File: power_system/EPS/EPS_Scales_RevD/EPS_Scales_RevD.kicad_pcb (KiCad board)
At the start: 4 copper layers, 100 x 100 mm, 268 parts, among them CN1 DF11-16DP-2DSA(08), J1 Input Power, J10 DF11-16DP-2DSA, J18 Conn_01x04, J2 Conn_01x01_Socket, J3 Conn_01x01_Socket, J4 Conn_01x01_Socket, J5 Conn_01x01_Socket, J6 DF11-16DP-2DSA, J7 Conn_01x04, J8 Conn_01x04, U1 LT8612EUDE#PBF, U12 TPS1HB08BQPWPRQ1, U13 LT8612EUDE#PBF, U14 TLV1704, U15 TPS1HB08BQPWPRQ1, U16 INA260AIPWR, U17 TPS1HB08BQPWPRQ1, U2 INA260AIPWR, U3 LT8612EUDE#PBF, U4 TLV1704, U5 INA260AIPWR, U6 TLV1704, U7 LTC6902, U9 TCA4307DGKR

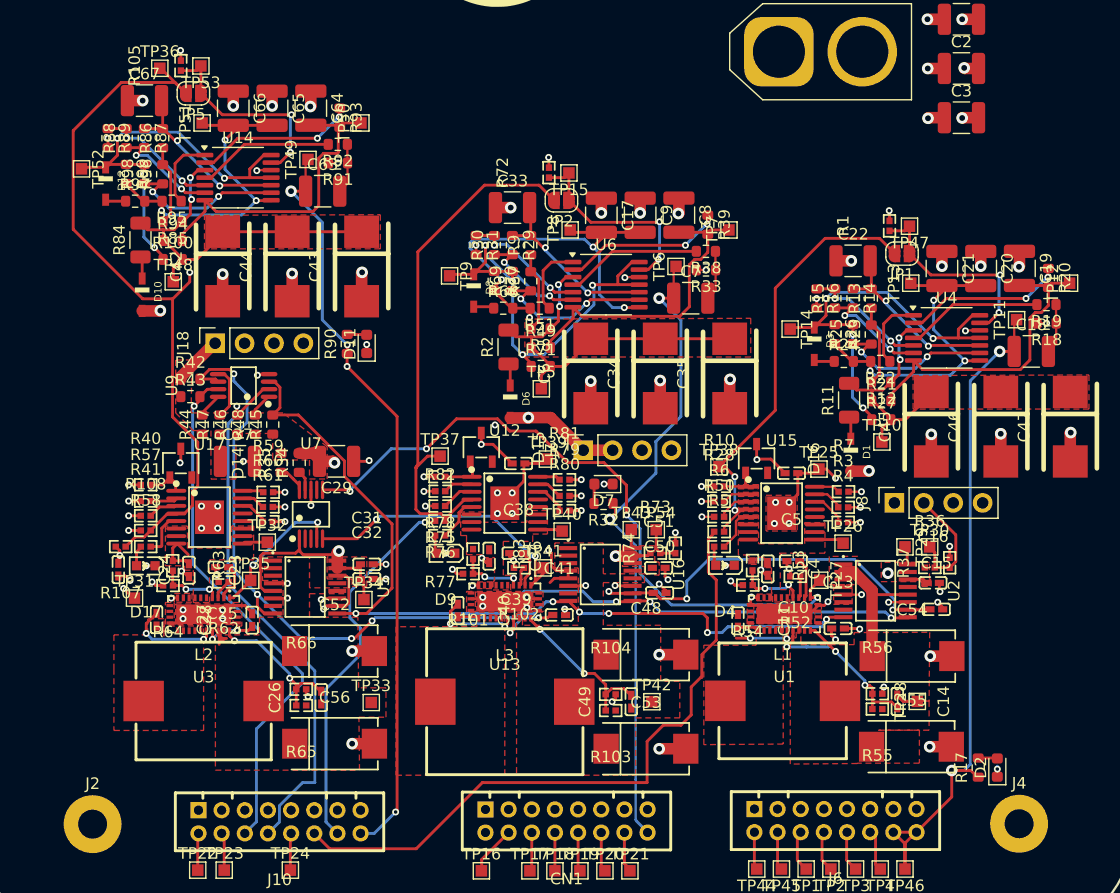
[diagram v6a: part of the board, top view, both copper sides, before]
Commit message: Cleaned up Layout
Fixed to work with JLC recommendations. Prepping for review with Andrew
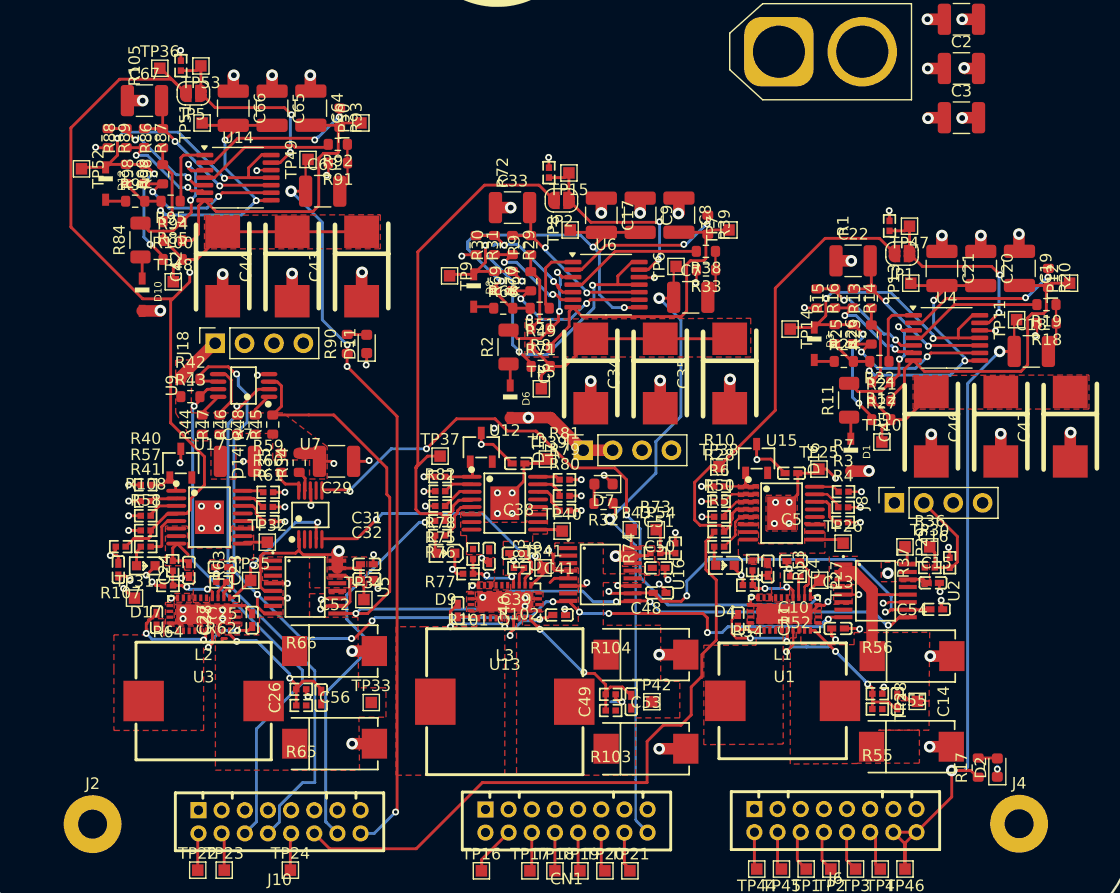
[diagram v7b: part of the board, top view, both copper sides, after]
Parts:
- moved R62 0.21 mm to (171.1, 96.1)
- moved R95 0.09 mm to (166.8, 63.2)
- moved U7 0.08 mm to (178.8, 90.3)
- moved C7 0.08 mm to (211.7, 71.5)
- moved R22 0.07 mm to (228.0, 77.0)
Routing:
- net GND: track 154.1 -> 160.4 mm, vias 116 -> 113
- net ~{WD_EN_JETSON}: track 39.1 -> 44.1 mm, vias 2 -> 0
- net Net-(U1-BST): track 5.07 -> 7.87 mm
- net Net-(U3-BIAS): track 3.77 -> 1.09 mm
- net /OBC_Subsystem/WD_OBC/WDT-VIN: track 31.9 -> 34.5 mm
- net SCL: track 79.4 -> 81.9 mm
- net /Perif_Subsystem/WD_Perif/WDT-VIN: track 32.1 -> 33.9 mm
- net Net-(U3-INTVCC): track 4.77 -> 6.46 mm
- net ~{WD_EN_OBC}: track 63.8 -> 65.4 mm
- net /Jetson_Subsystem/WD_Jetson/WDT-VIN: track 19.9 -> 21.2 mm
- net Net-(D12-K): track 35.5 -> 36.6 mm
- net +3.3V_OBC: track 113.3 -> 112.3 mm
- net Net-(U15-SEL1): track 3.02 -> 4.06 mm
- net ~{WD_EN_PERIF}: track 45.9 -> 46.9 mm
- net Net-(D3-K): track 35.5 -> 36.4 mm
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
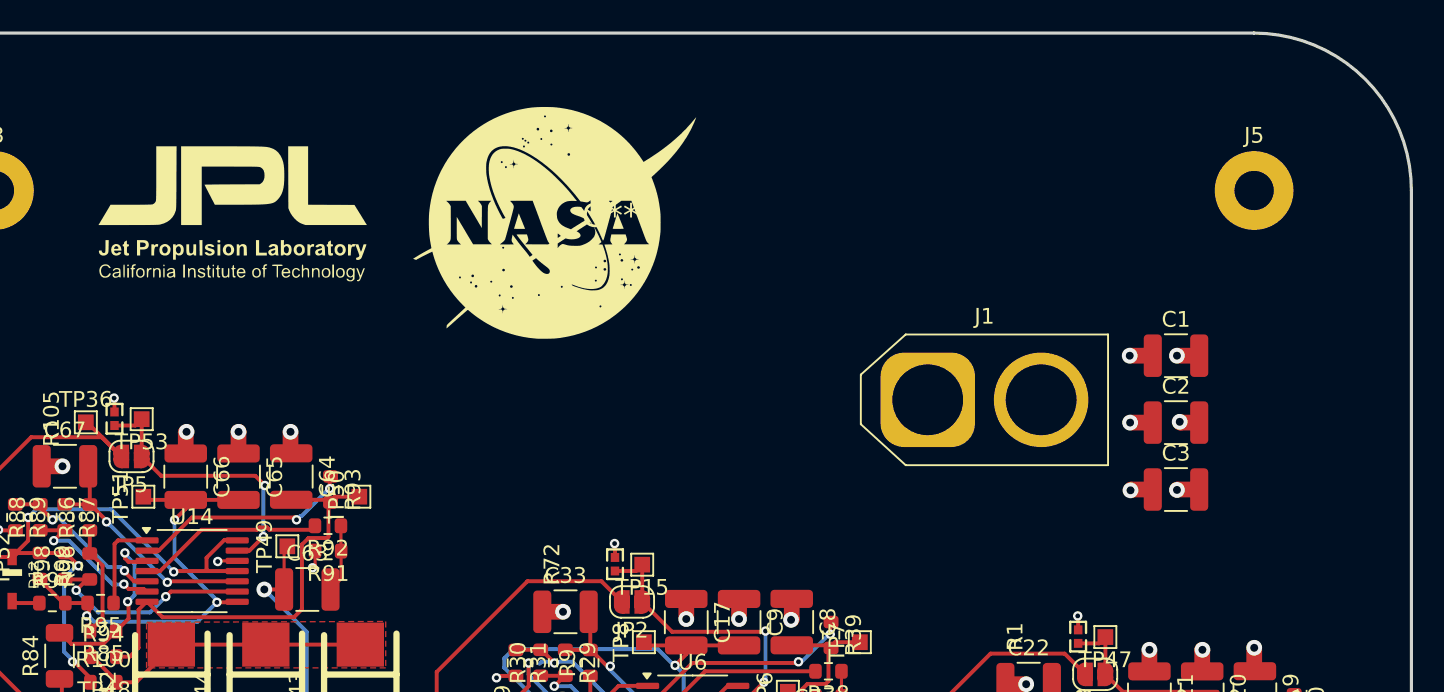
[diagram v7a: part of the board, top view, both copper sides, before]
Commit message: Added some more things to Layout
Added XT-60 Female Right Angle connector
Added 3d models to almost every component
Added meme image to board.
Board is complete. Awaiting review with Andrew Greenberg @2pm
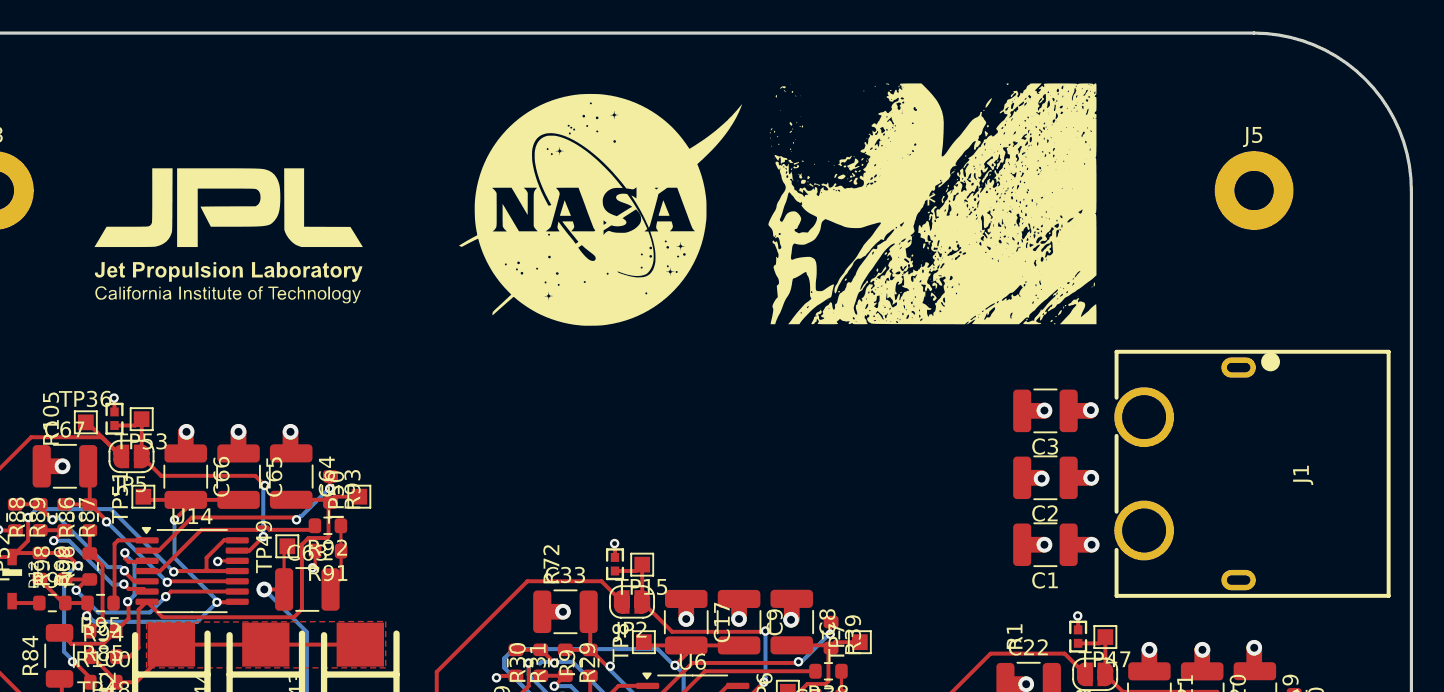
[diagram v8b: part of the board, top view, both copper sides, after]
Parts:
- added G***: LOGO, LOGO, F.Cu at (217.5, 37.8)
- J1: footprint Connector_AMASS:AMASS_XT60-M_1x02_P7.20mm_Vertical -> EPS:TH_2P-XT60PW-F
- moved J1 17.4 mm to (236.0, 55.0), turned to -90 degrees
- moved C1 14.6 mm to (226.8, 59.5), turned to 180 degrees
- moved C3 9.68 mm to (226.8, 51.0), turned to 180 degrees
- moved C2 9.00 mm to (226.8, 55.2), turned to 180 degrees
- moved G*** 3.03 mm to (198.1, 38.2)
- moved G*** 1.42 mm to (174.9, 39.9)
